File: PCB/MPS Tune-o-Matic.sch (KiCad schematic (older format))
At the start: 18 parts

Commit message: WIP
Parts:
- removed D?: RED, LED_SMD:LED_PLCC-2, symbol Device:LED
- removed R?: 1K, Resistor_SMD:R_0805_2012Metric, symbol Device:R
- added J?: UI, symbol Connector_Generic:Conn_01x12
- added J?: GND, symbol Connector_Generic:Conn_01x04
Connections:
- net labels added: ENABLE_II_IV, LCD_DC_X+, MIXTURE_BIAS, MIXTURE_BIAS_12V, MPS-7_MCU, X-, Y+, Y-, ~LCD_CS, ~SD_CS
- net labels removed: BASE_INJECTOR_PULSE, ECU_AIRTEMP, STATUS
- wire segments 111 -> 122
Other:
- note added: "MPS-7 is the base injector pulse"
- note added: "Y+ and X- are analog\nY- and X+ are digital"
- note removed: "Add 10V regulator\n"
- note removed: "Min 3A connector"
- moved on the sheet: J?

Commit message: WIP.
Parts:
- removed J?: UI, symbol Connector_Generic:Conn_01x12
- added J?: UI1, Connector_JST:JST_PH_B8B-PH-K_1x08_P2.00mm_Vertical, symbol Connector_Generic:Conn_01x08
- added J?: UI2, Connector_JST:JST_PH_B4B-PH-K_1x04_P2.00mm_Vertical, symbol Connector_Generic:Conn_01x04
- J?: footprint (none) -> Connector_PinHeader_2.54mm:PinHeader_1x06_P2.54mm_Vertical
- J?: footprint (none) -> Connector_PinHeader_2.54mm:PinHeader_1x04_P2.54mm_Vertical
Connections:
- wire segments 122 -> 125
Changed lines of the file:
@@
 F 0 "J?" H 9330 3692 50  0000 L CNN
 F 1 "MPS BREAKOUT" H 9330 3601 50  0000 L CNN
-F 2 "" H 9250 3700 50  0001 C CNN
+F 2 "Connector_PinHeader_2.54mm:PinHeader_1x06_P2.54mm_Vertical" H 9250 3700 50  0001 C CNN
 F 3 "~" H 9250 3700 50  0001 C CNN
 	1    9250 3700
@@
 Text Label 10350 2050 2    50   ~ 0
 ~LCD_CS
+Text Label 10350 2450 2    50   ~ 0
+SCK
 Text Label 10350 2350 2    50   ~ 0
-SCK
-Text Label 10350 2250 2    50   ~ 0
 MISO
 Text Label 10350 2150 2    50   ~ 0
@@
 Y-
 $Comp
-L Connector_Generic:Conn_01x12 J?
-U 1 1 61AF7172
-P 10550 1950
-F 0 "J?" H 10630 1942 50  0000 L CNN
-F 1 "UI" H 10630 1851 50  0000 L CNN
-F 2 "" H 10550 1950 50  0001 C CNN
-F 3 "~" H 10550 1950 50  0001 C CNN
-	1    10550 1950
-	1    0    0    -1
-$EndComp
-$Comp
 L power:+5V #PWR?
 U 1 1 61AFDEC3
@@
 L power:GND #PWR?
 U 1 1 61AFE287
-P 10200 2800
-F 0 "#PWR?" H 10200 2550 50  0001 C CNN
-F 1 "GND" H 10205 2627 50  0000 C CNN
-F 2 "" H 10200 2800 50  0001 C CNN
-F 3 "" H 10200 2800 50  0001 C CNN
-	1    10200 2800
-	1    0    0    -1
-$EndComp
-Wire Wire Line
-	10200 2800 10200 2550
-Wire Wire Line
-	10200 2550 10350 2550
-Wire Wire Line
-	9800 2450 9800 1200
+P 10200 2900
+F 0 "#PWR?" H 10200 2650 50  0001 C CNN
+F 1 "GND" H 10205 2727 50  0000 C CNN
+F 2 "" H 10200 2900 50  0001 C CNN
+F 3 "" H 10200 2900 50  0001 C CNN
+	1    10200 2900
+	1    0    0    -1
+$EndComp
+Wire Wire Line
+	10200 2900 10200 2650
+Wire Wire Line
+	10200 2650 10350 2650
 Text Label 10350 1950 2    50   ~ 0
 LCD_DC_X+
 Wire Wire Line
-	9800 2450 10350 2450
+	9800 2550 10350 2550
 $Sheet
 S 1550 6100 2050 650
@@
 F4 "SPEED_SENSOR_PULSE_12V" O R 3600 6200 50
 F5 "ENABLE_II_IV_12V" O R 3600 6300 50
+F6 "MIXTURE_BIAS" I L 1550 6400 50
+F7 "MIXTURE_BIAS_12V" O R 3600 6400 50
 $EndSheet
 Wire Wire Line
@@
 F 0 "J?" H 10680 3692 50  0000 L CNN
 F 1 "GND" H 10680 3601 50  0000 L CNN
-F 2 "" H 10600 3700 50  0001 C CNN
+F 2 "Connector_PinHeader_2.54mm:PinHeader_1x04_P2.54mm_Vertical" H 10600 3700 50  0001 C CNN
 F 3 "~" H 10600 3700 50  0001 C CNN
 	1    10600 3700
@@
 Wire Wire Line
 	10250 3700 10250 3800
-Text Label 3750 6600 0    50   ~ 0
+Text Label 3700 6400 0    50   ~ 0
 MIXTURE_BIAS_12V
-Text Label 1400 6650 2    50   ~ 0
+Text Label 1450 6400 2    50   ~ 0
 MIXTURE_BIAS
 Wire Wire Line
@@
 Wire Wire Line
 	4750 1900 4550 1900
-Text Notes 6200 5250 0    50   ~ 0
+Text Notes 6650 5250 0    50   ~ 0
 MPS-7 is the base injector pulse
 $Sheet
@@
 F0 "Input Drivers" 50
 F1 "Input Drivers.sch" 50
+F2 "MPS-7" I L 8050 5500 50
+F3 "MP-7_MCU" O R 9700 5500 50
 $EndSheet
-Wire Wire Line
-	6600 5500 7850 5500
-Text Label 9950 5500 0    50   ~ 0
+Text Label 9800 5500 0    50   ~ 0
 MPS-7_MCU
 Text Notes 5350 2550 0    50   ~ 0
@@
 Text Label 5350 3000 0    50   ~ 0
 MIXTURE_BIAS
+$Comp
+L Connector_Generic:Conn_01x08 J?
+U 1 1 61AF45AA
+P 10550 1750
+F 0 "J?" H 10630 1742 50  0000 L CNN
+F 1 "UI1" H 10630 1651 50  0000 L CNN
+F 2 "Connector_JST:JST_PH_B8B-PH-K_1x08_P2.00mm_Vertical" H 10550 1750 50  0001 C CNN
+F 3 "~" H 10550 1750 50  0001 C CNN
+	1    10550 1750
+	1    0    0    -1
+$EndComp
+$Comp
+L Connector_Generic:Conn_01x04 J?
+U 1 1 61AF519E
+P 10550 2450
+F 0 "J?" H 10630 2442 50  0000 L CNN
+F 1 "UI2" H 10630 2351 50  0000 L CNN
+F 2 "Connector_JST:JST_PH_B4B-PH-K_1x04_P2.00mm_Vertical" H 10550 2450 50  0001 C CNN
+F 3 "~" H 10550 2450 50  0001 C CNN
+	1    10550 2450
+	1    0    0    -1
+$EndComp
+Wire Wire Line
+	9800 1200 9800 2550
+Wire Wire Line
+	1450 6400 1550 6400
+Wire Wire Line
+	3700 6400 3600 6400
+Wire Wire Line
+	6600 5500 8050 5500
+Wire Wire Line
+	9700 5500 9800 5500
 $EndSCHEMATC

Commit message: WIP
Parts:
- removed J?: MPS, Britishideas:PhoenixContact_COMBICON_PT_4, symbol Connector:Screw_Terminal_01x04
- removed J?: 12V IN, Britishideas:PhoenixContact_COMBICON_MKDSN_2, symbol Connector:Screw_Terminal_01x02
- removed J?: MPS BREAKOUT, Connector_PinHeader_2.54mm:PinHeader_1x06_P2.54mm_Vertical, symbol Connector_Generic:Conn_01x06
- removed J?: GND, Connector_PinHeader_2.54mm:PinHeader_1x04_P2.54mm_Vertical, symbol Connector_Generic:Conn_01x04
- added J?: DB9_Male, symbol Connector:DB9_Male
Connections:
- net +5V: now also J?.5
- net GND: now also J?.3
- net MPS-15: now also J?.1
- net MPS-7: now also J?.7
- net MPS-8: now also J?.2
- net ENABLE_II_IV: no longer names the net of U?.27 (PC4(ADC4/SDA))
- net SPEED_SENSOR_PULSE: no longer names the net of U?.13 (PB1(OC1A))
- net ~AIRTEMP_CS: no longer names the net of U?.28 (PC5(ADC5/SCL))
- new net IO0: J?.9
- new net IO1: J?.4
- new net IO2: J?.8
- new net MPS-10: J?.6
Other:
- note removed: "MPS-7 is the base injector pulse"
- moved on the sheet: C?, R?, U?, Y?

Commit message: WIP.
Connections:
- net IO0: now also U?.1 (PD3(INT1))
- net IO1: now also U?.2 (PD4(XCK/T0))
- net IO2: now also U?.9 (PD5(T1))
- net MPS_PULSE: now also U?.32 (PD2(INT0))
- net MPS_STIMULUS: now also U?.13 (PB1(OC1A))
- no-connect marks 0 -> 5
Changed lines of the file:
@@
 Wire Wire Line
 	4700 6550 4600 6550
-Text Label 6050 2500 0    50   ~ 0
+Text Label 5450 2500 0    50   ~ 0
 MPS_STIMULUS
-Text Label 5750 3600 0    50   ~ 0
+Text Label 5450 3800 0    50   ~ 0
 MPS_PULSE
 Text Label 4700 6700 0    50   ~ 0
@@
 Wire Wire Line
 	9850 4450 10000 4450
-Text Label 6150 2750 0    50   ~ 0
+Text Label 5450 3700 0    50   ~ 0
 IO0
-Text Label 6150 2850 0    50   ~ 0
+Text Label 5450 3600 0    50   ~ 0
 IO1
-Text Label 6150 2950 0    50   ~ 0
+Text Label 5450 3500 0    50   ~ 0
 IO2
+Wire Wire Line
+	5450 2500 5250 2500
+Wire Wire Line
+	5450 3800 5250 3800
+Wire Wire Line
+	5450 3500 5250 3500
+Wire Wire Line
+	5250 3600 5450 3600
+Wire Wire Line
+	5450 3700 5250 3700
+NoConn ~ 5250 2700
+NoConn ~ 5250 2800
+NoConn ~ 5250 3000
+NoConn ~ 3600 3200
+NoConn ~ 3600 3100
 $EndSCHEMATC

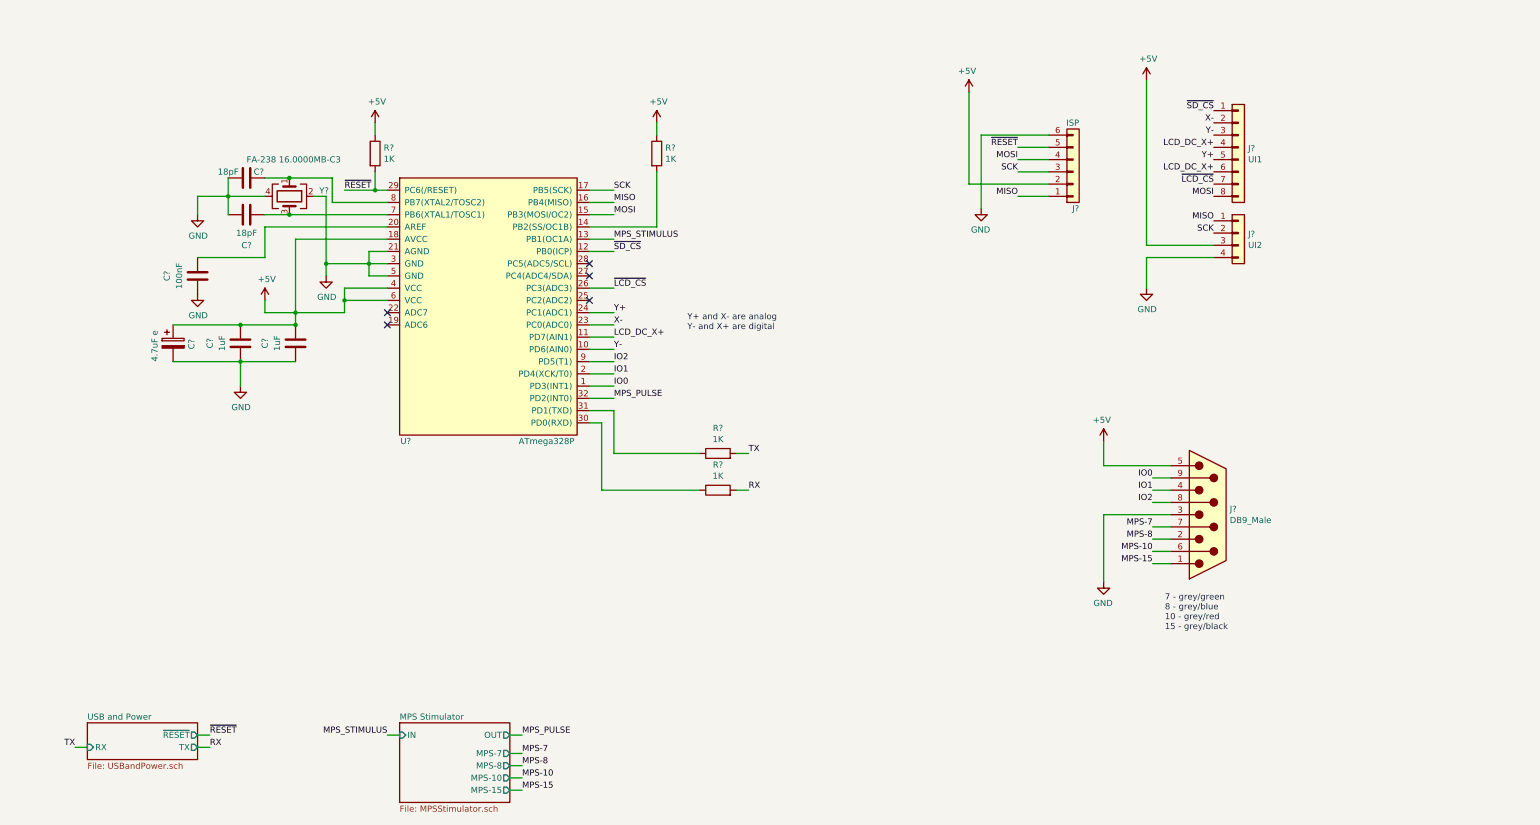
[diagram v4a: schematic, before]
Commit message: Completed schematic. Started work on PCB.
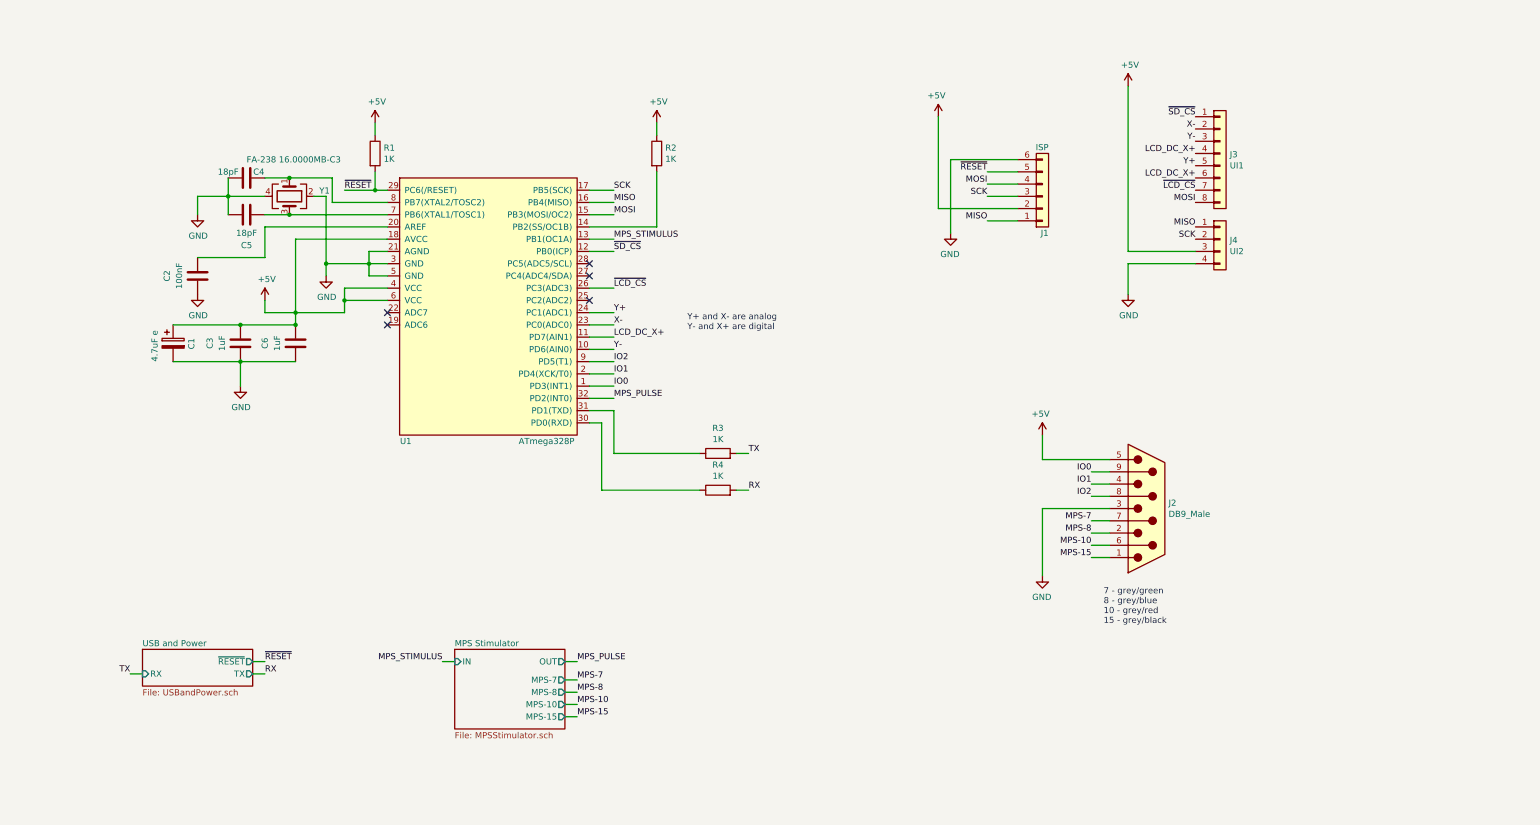
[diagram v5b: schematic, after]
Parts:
- C2, C3, C4, C5, C6: renamed from C?; footprint Capacitor_SMD:C_0805_2012Metric -> Capacitor_SMD:C_0603_1608Metric
- J2: renamed from J?; footprint (none) -> EmSA:DB9_RA_MALE_LD09P13A4
- R1, R2, R3, R4: renamed from R?; footprint Resistor_SMD:R_0805_2012Metric -> Resistor_SMD:R_0603_1608Metric
- gave numbers to parts that had none: 6
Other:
- moved on the sheet: J1, J2, J3, J4

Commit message: Working on PCB layout.
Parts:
- C1: footprint Capacitor_SMD:CP_Elec_4x5.8 -> Capacitor_SMD:C_0603_1608Metric
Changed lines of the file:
@@
 F 0 "C1" V 2000 3300 50  0000 L CNN
 F 1 "4.7uF e" V 1700 3200 50  0000 L CNN
-F 2 "Capacitor_SMD:CP_Elec_4x5.8" H 1888 3200 50  0001 C CNN
+F 2 "Capacitor_SMD:C_0603_1608Metric" H 1888 3200 50  0001 C CNN
 F 3 "~" H 1850 3350 50  0001 C CNN
 	1    1850 3350

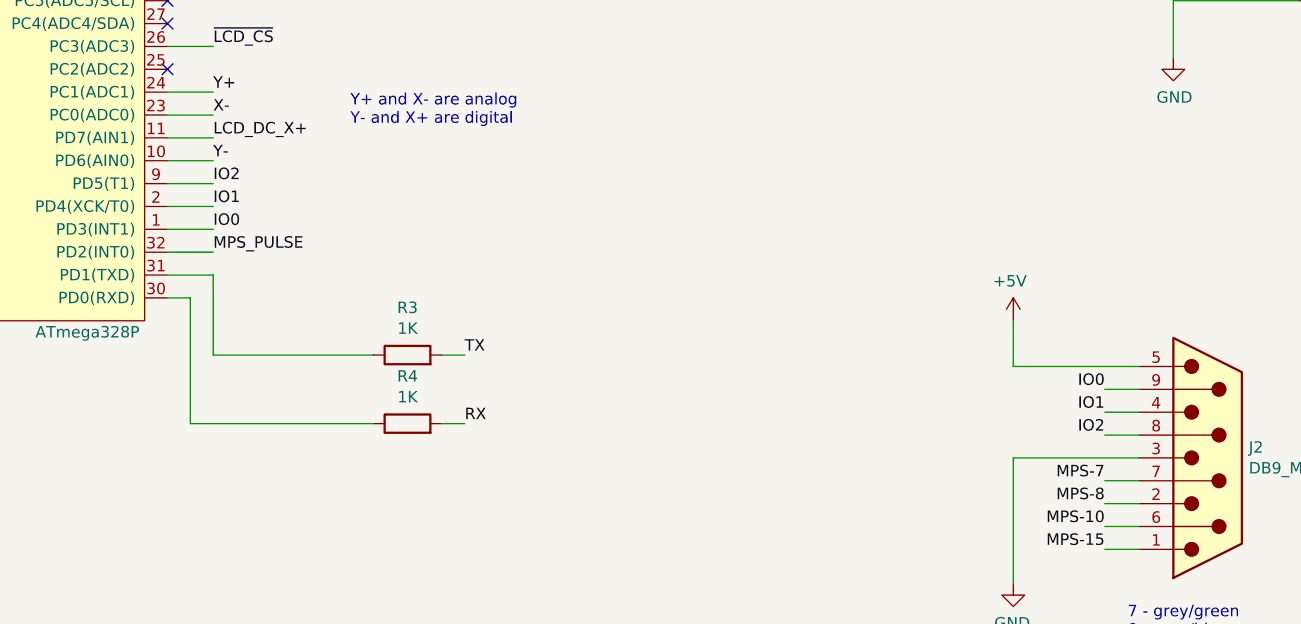
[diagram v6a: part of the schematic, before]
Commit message: Completed PCB layout.
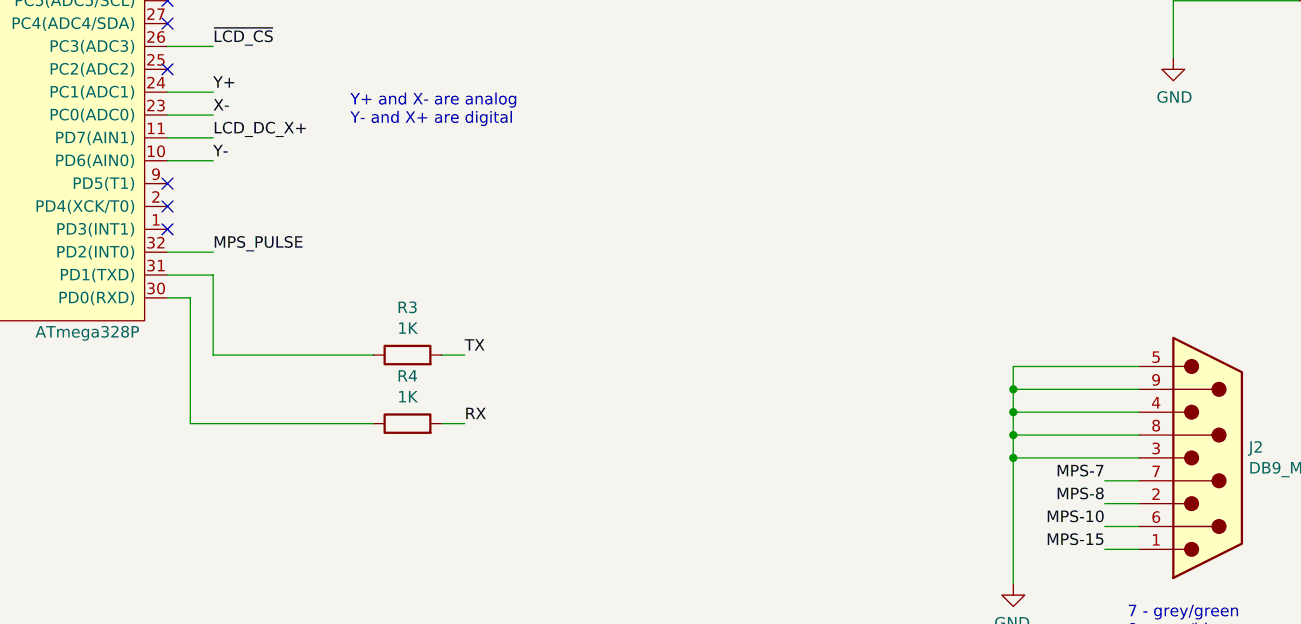
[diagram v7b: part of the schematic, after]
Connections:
- net +5V: no longer J2.5
- net GND: now also J2.4, J2.5, J2.8, J2.9
- net IO0: no longer names the net of U1.1 (PD3(INT1))
- net IO0: no longer J2.9
- net IO1: no longer names the net of U1.2 (PD4(XCK/T0))
- net IO1: no longer J2.4
- net IO2: no longer names the net of U1.9 (PD5(T1))
- net IO2: no longer J2.8
- no-connect marks 5 -> 8
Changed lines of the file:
@@
 $EndComp
-Wire Wire Line
-	8950 4100 8950 4300
-Wire Wire Line
-	8950 4300 9500 4300
 Wire Wire Line
 	8950 5250 8950 4700
 Wire Wire Line
 	8950 4700 9500 4700
-$Comp
-L power:+5V #PWR010
-U 1 1 6214D24D
-P 8950 4100
-F 0 "#PWR010" H 8950 3950 50  0001 C CNN
-F 1 "+5V" H 8965 4273 50  0000 C CNN
-F 2 "" H 8950 4100 50  0001 C CNN
-F 3 "" H 8950 4100 50  0001 C CNN
-	1    8950 4100
-	-1   0    0    -1
-$EndComp
 Text Label 4050 5950 2    50   ~ 0
 MPS_STIMULUS
@@
 Wire Wire Line
 	5050 6100 5150 6100
-Text Label 9350 4400 2    50   ~ 0
-IO0
-Text Label 9350 4500 2    50   ~ 0
-IO1
-Text Label 9350 4600 2    50   ~ 0
-IO2
-Wire Wire Line
-	9350 4600 9500 4600
-Wire Wire Line
-	9500 4500 9350 4500
-Wire Wire Line
-	9350 4400 9500 4400
-Text Label 5450 3700 0    50   ~ 0
-IO0
-Text Label 5450 3600 0    50   ~ 0
-IO1
-Text Label 5450 3500 0    50   ~ 0
-IO2
 Wire Wire Line
 	5450 2500 5250 2500
 Wire Wire Line
 	5450 3800 5250 3800
-Wire Wire Line
-	5450 3500 5250 3500
-Wire Wire Line
-	5250 3600 5450 3600
-Wire Wire Line
-	5450 3700 5250 3700
 NoConn ~ 5250 2700
 NoConn ~ 5250 2800
@@
 NoConn ~ 3600 3200
 NoConn ~ 3600 3100
+Wire Wire Line
+	8950 4300 9500 4300
+Wire Wire Line
+	8950 4300 8950 4400
+Connection ~ 8950 4700
+Wire Wire Line
+	9500 4400 8950 4400
+Connection ~ 8950 4400
+Wire Wire Line
+	8950 4400 8950 4500
+Wire Wire Line
+	9500 4500 8950 4500
+Connection ~ 8950 4500
+Wire Wire Line
+	8950 4500 8950 4600
+Wire Wire Line
+	9500 4600 8950 4600
+Connection ~ 8950 4600
+Wire Wire Line
+	8950 4600 8950 4700
+NoConn ~ 5250 3500
+NoConn ~ 5250 3600
+NoConn ~ 5250 3700
 $EndSCHEMATC

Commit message: Added status LED, remove LCD connectors, changed MPS connector to screw terminal block, added 12V power connections, removed 5V to 12V boost converter. Completely reworked PCB. Removed old PCB CAD files.
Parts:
- removed J2: DB9_Male, EmSA:DB9_RA_MALE_LD09P13A4, symbol Connector:DB9_Male
- removed J3: UI1, Connector_JST:JST_PH_B8B-PH-K_1x08_P2.00mm_Vertical, symbol Connector_Generic:Conn_01x08
- removed J4: UI2, Connector_JST:JST_PH_B4B-PH-K_1x04_P2.00mm_Vertical, symbol Connector_Generic:Conn_01x04
- added D8: APT1608EC, LED_SMD:LED_0603_1608Metric, symbol Device:LED
- added J2: MPS, Britishideas:PhoenixContact_COMBICON_PT_4, symbol Connector:Screw_Terminal_01x04
- added R29: 150, Resistor_SMD:R_0603_1608Metric, symbol Device:R
- U1: symbol BritishIdeas:ATmega328P -> MPS-Tune-o-Matic-rescue:ATmega328P-BritishIdeas
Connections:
- net +5V: now also D8.2 (A)
- net MPS-10: now also J2.3 (Pin_3)
- net MPS-15: now also J2.4 (Pin_4)
- net MPS-7: now also J2.1 (Pin_1)
- net MPS-8: now also J2.2 (Pin_2)
- net LCD_DC_X+: no longer names the net of U1.11 (PD7(AIN1))
- net X-: no longer names the net of U1.23 (PC0(ADC0))
- net Y+: no longer names the net of U1.24 (PC1(ADC1))
- net Y-: no longer names the net of U1.10 (PD6(AIN0))
- net ~LCD_CS renamed STATUS
- net STATUS: now also R29.1
- net ~SD_CS: no longer names the net of U1.12 (PB0(ICP))
- new net: D8.1 (K), R29.2
- no-connect marks 8 -> 13
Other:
- note removed: "Y+ and X- are analog\nY- and X+ are digital"
- moved on the sheet: J1
